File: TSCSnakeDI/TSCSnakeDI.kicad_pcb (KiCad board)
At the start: 2 copper layers, 76.2 x 50.8 mm, 22 parts, among them J1 CH 1 IN, J2 ST IN, J3 CH 1 OUT, J4 CH 2 IN, J5 ST IN, J6 CH 2 OUT, T1 JT-DB-EPC, T2 JT-DB-EPC

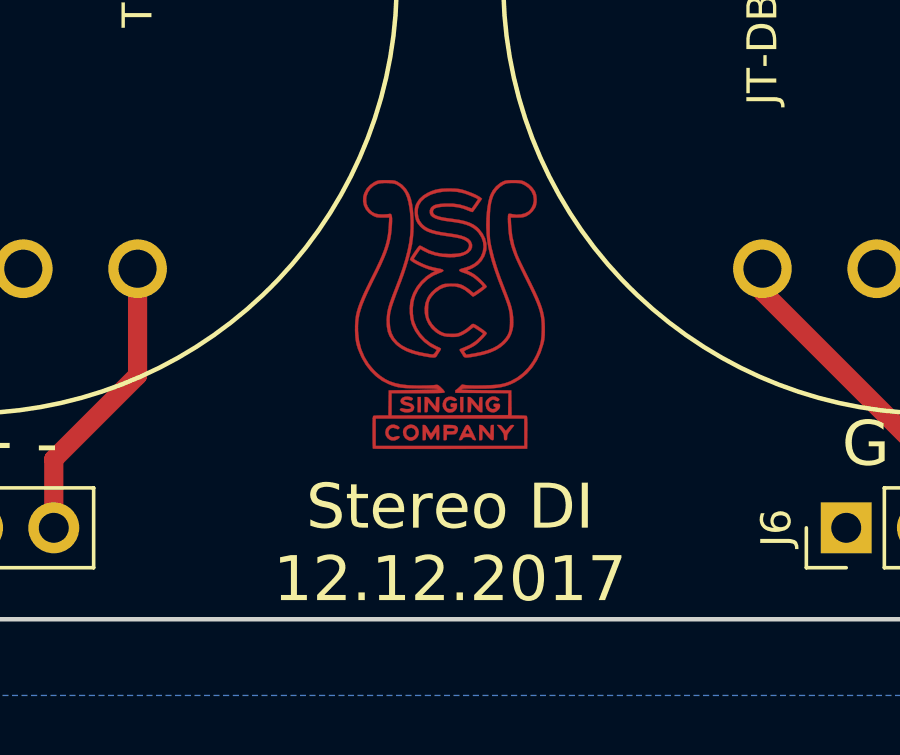
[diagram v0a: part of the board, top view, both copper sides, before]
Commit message: Remove logo & link DI PCB
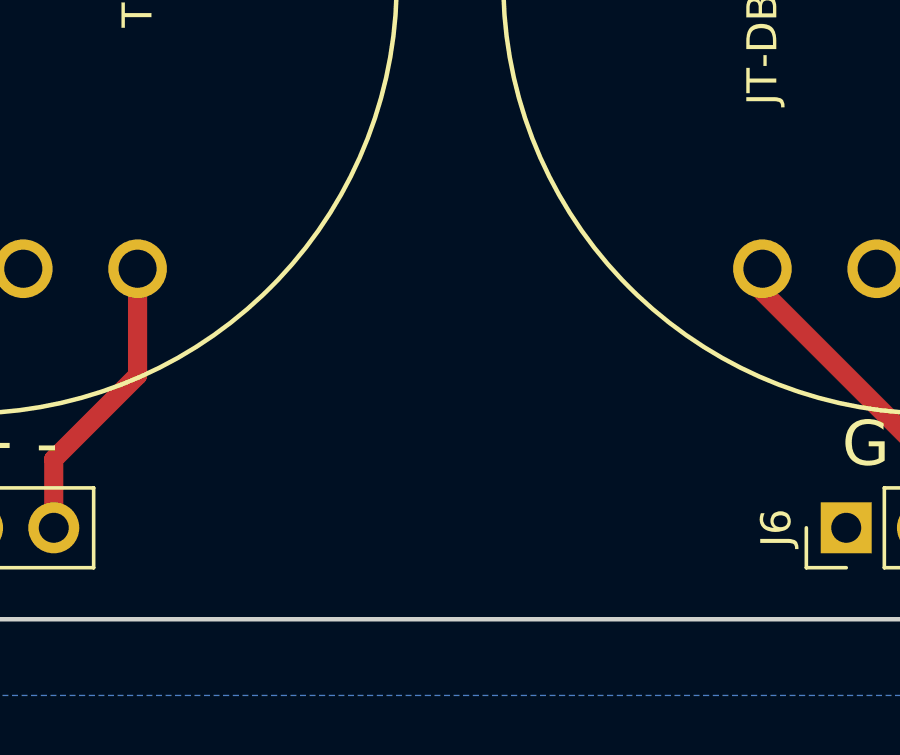
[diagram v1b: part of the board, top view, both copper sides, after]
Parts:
- removed G***: LOGO, logo:TSC
- removed G***: LOGO, logo:TSCMask
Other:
- board text removed: "Stereo DI 12.12.2017"
